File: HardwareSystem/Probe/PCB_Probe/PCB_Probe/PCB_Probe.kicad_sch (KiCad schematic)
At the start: 24 parts, among them J1 Conn_01x15, J2 Conn_01x15, U1 TLC555xP, U2 LP2950CZ-3.0/NOPB

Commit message: PCB Probe layout
working on pcb probe layout
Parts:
- removed R7: Photoresistor, KiCADv6:XDCR_161, symbol 161:Photoresistor
- added J3: Conn_01x02_Socket, Connector_PinHeader_2.54mm:PinHeader_1x02_P2.54mm_Vertical, symbol Connector:Conn_01x02_Socket
- added J4: Conn_01x04_Pin, Connector_PinHeader_2.54mm:PinHeader_1x04_P2.54mm_Vertical, symbol Connector:Conn_01x04_Pin
- added TP4: 3.3V GND Testpoint, TestPoint:TestPoint_Pad_D1.0mm, symbol Connector:TestPoint
- A2: now not fitted
- TP1: value 5V Testpoint -> 9V Testpoint
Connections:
- net +3.3V: now also J3.1 (Pin_1), J4.1 (Pin_1)
- net GND: now also J4.2 (Pin_2), TP4.1
- net SCL: now also J4.3 (Pin_3)
- net SDA: now also J4.4 (Pin_4)
- net at R6.2: now also J3.2 (Pin_2)
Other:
- note added: "AHT20 Temp Humd connection"
- moved on the sheet: BT1, C1, C10, C2, C3, C4, C9, D1, J1, J2, R1, R2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

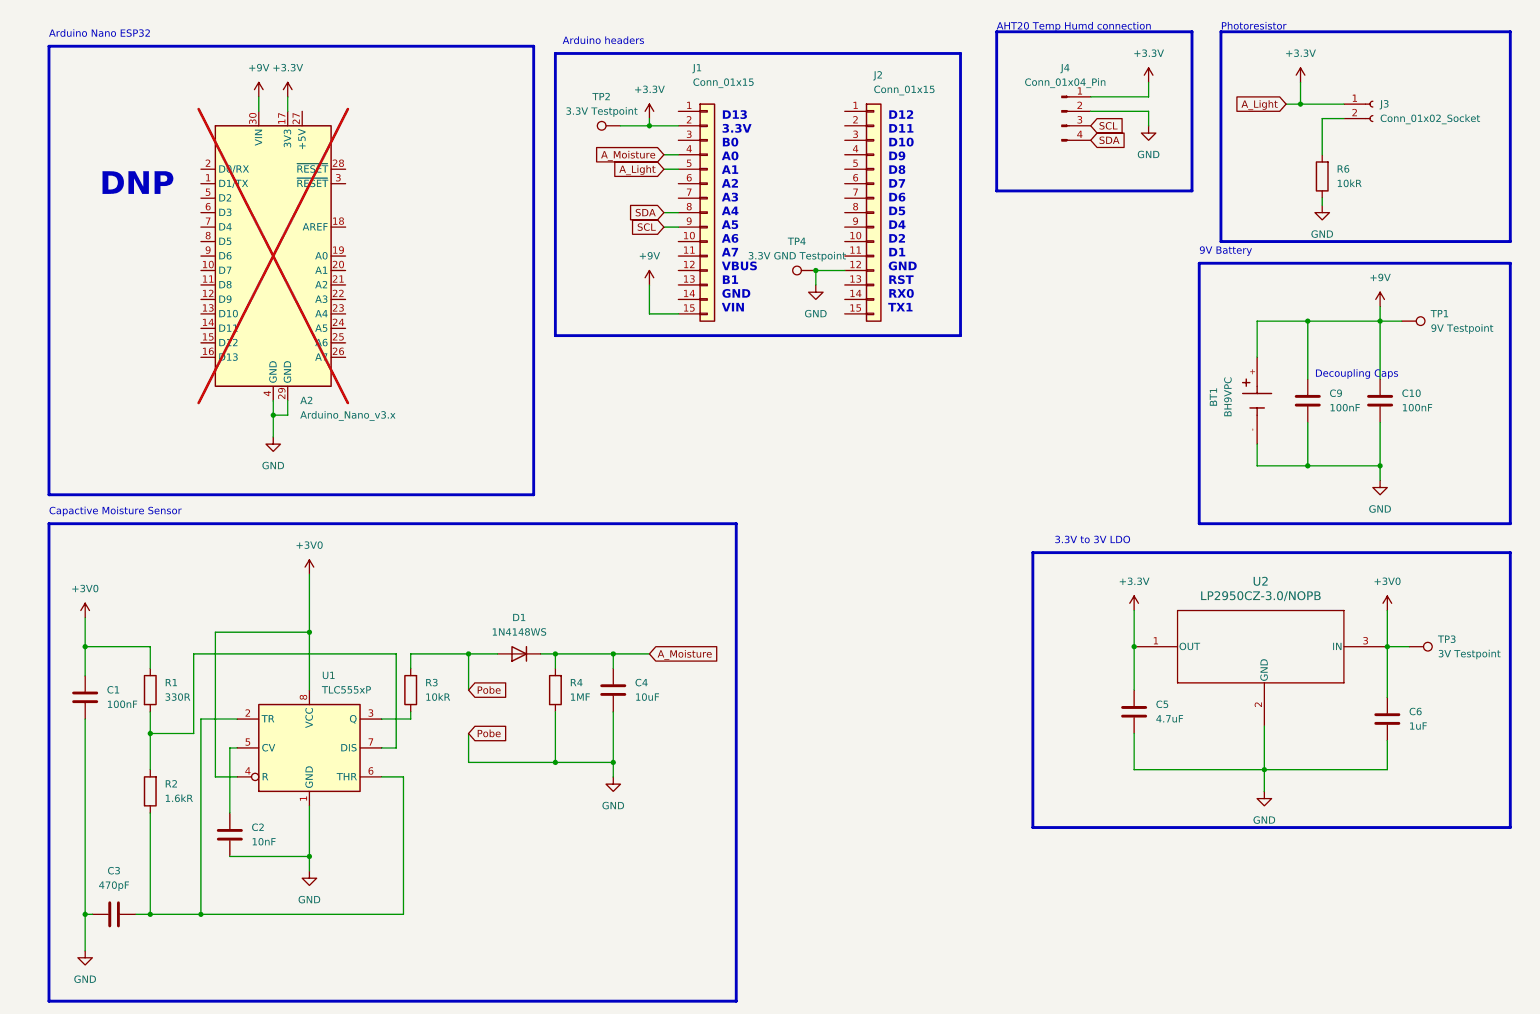
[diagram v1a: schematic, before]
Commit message: Routing and Placement for Probe PCB
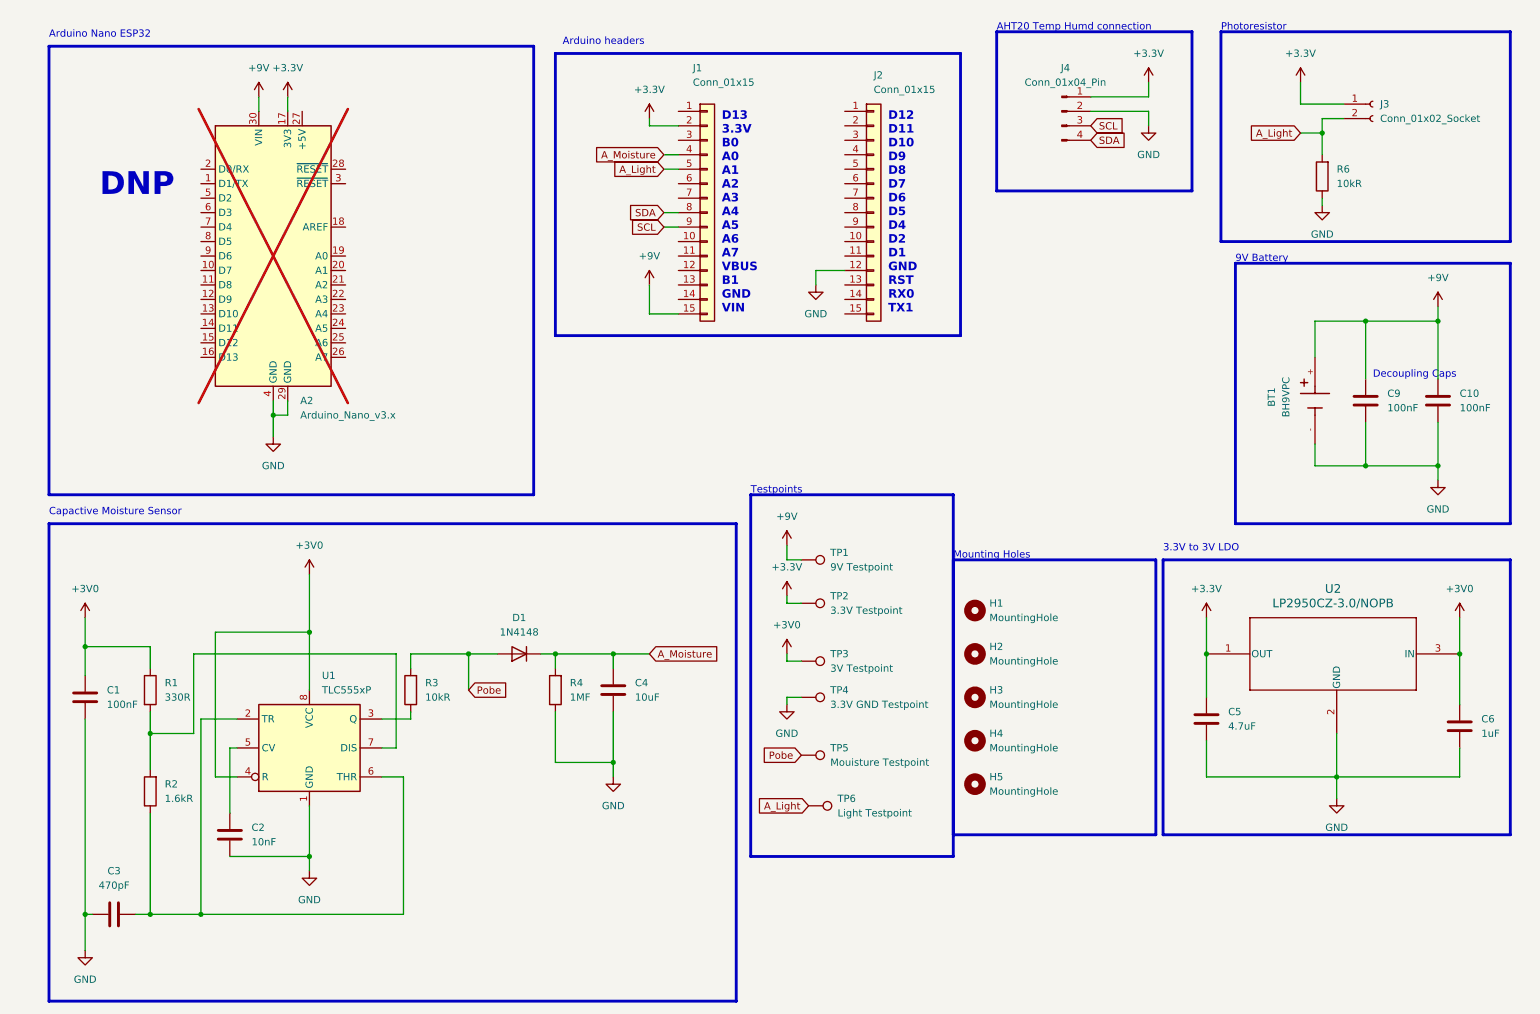
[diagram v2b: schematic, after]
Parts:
- removed D1: 1N4148WS, Diode_SMD:D_SOD-323, symbol Diode:1N4148WS
- added D1: 1N4148, Diode_THT:D_DO-35_SOD27_P7.62mm_Horizontal, symbol Diode:1N4148
- added H1, H2, H3, H4, H5: MountingHole, MountingHole:MountingHole_3.2mm_M3, symbol Mechanical:MountingHole
- added TP5: Mouisture Testpoint, TestPoint:TestPoint_Pad_D1.0mm, symbol Connector:TestPoint
- added TP6: Light Testpoint, TestPoint:TestPoint_Pad_D1.0mm, symbol Connector:TestPoint
- A2: now left out of the parts list
- C1, C10, C2, C3, C4, C5, C6, C9: footprint Capacitor_THT:C_Disc_D3.0mm_W1.6mm_P2.50mm -> Capacitor_THT:C_Disc_D4.7mm_W2.5mm_P5.00mm
- R1, R2, R3, R4, R6: footprint Resistor_THT:R_Axial_DIN0204_L3.6mm_D1.6mm_P5.08mm_Horizontal -> Resistor_THT:R_Axial_DIN0207_L6.3mm_D2.5mm_P10.16mm_Horizontal
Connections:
- net +3.3V: no longer J1.5 (Pin_5)
- net A_Moisture: now also D1.1 (K)
- net GND: no longer R3.2
- net A_Light: now reaches J3.2 (Pin_2), R6.2
- net A_Light: now also J1.5 (Pin_5), TP6.1
- new net Pobe: D1.2 (A), R3.2, TP5.1
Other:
- note added: "Mounting Holes"
- note added: "Testpoints"
- moved on the sheet: BT1, C10, C5, C6, C9, TP2, U2

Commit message: updated Probe schematic look
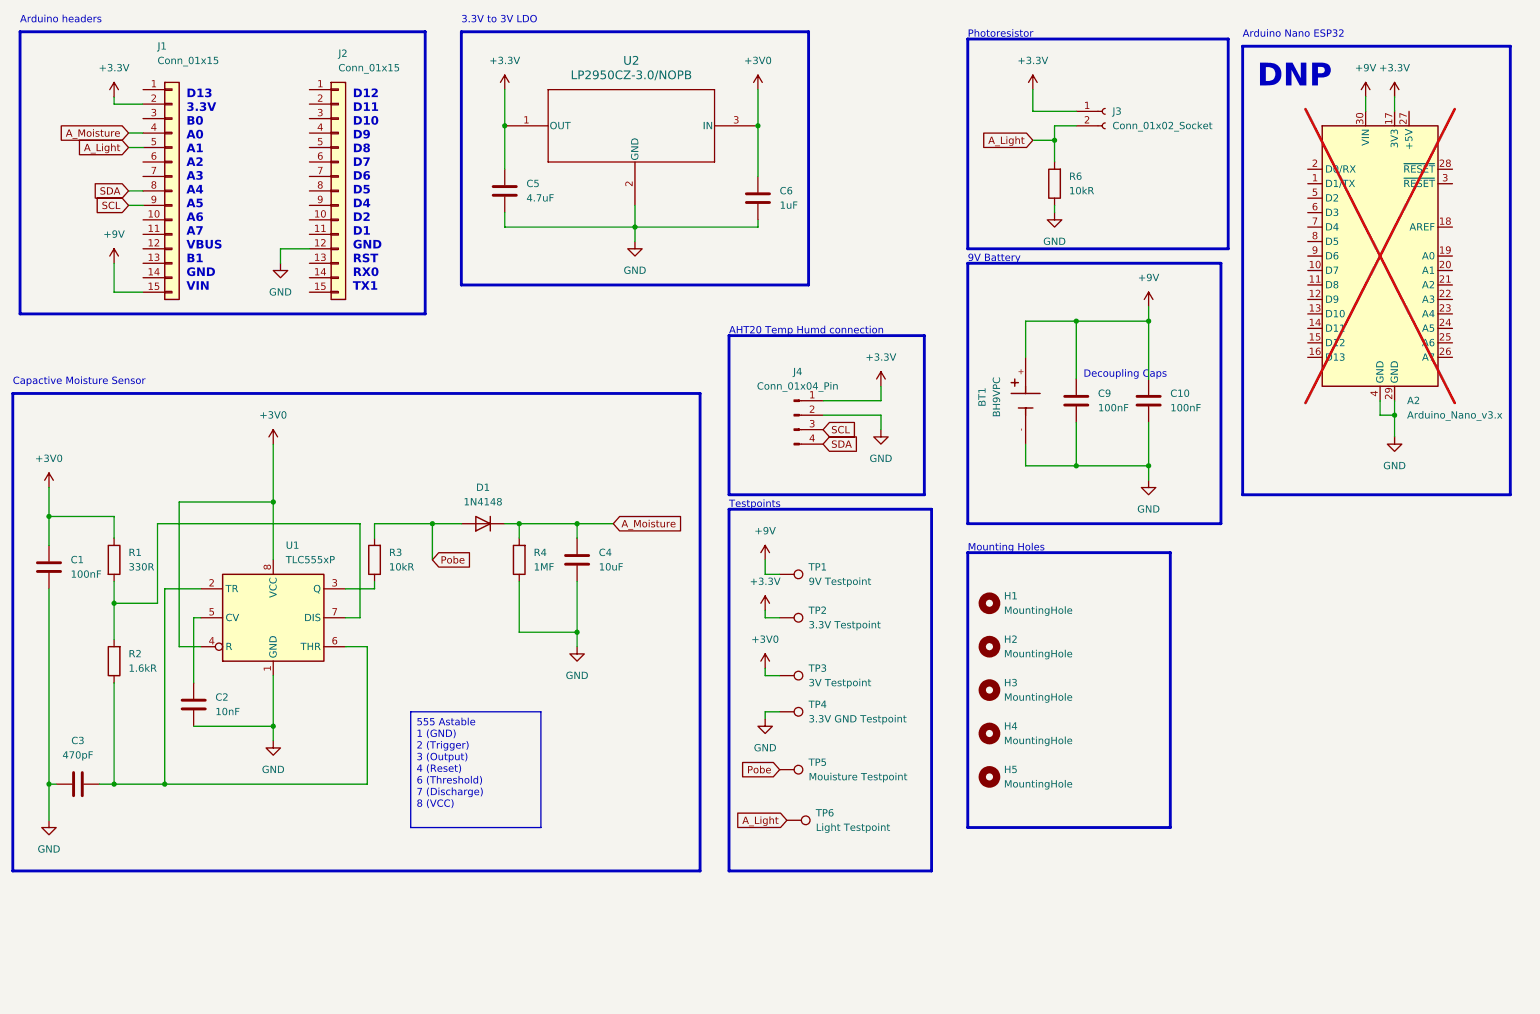
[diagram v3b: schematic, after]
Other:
- moved on the sheet: A2, BT1, C1, C10, C2, C3, C4, C5, C6, C9, D1, H1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

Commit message: updated ground plane footprint
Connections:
- net Pobe renamed Probe
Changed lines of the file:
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@@
     )
   )
-  (global_label "Pobe" (shape input) (at 154.94 147.32 180) (fields_autoplaced)
+  (global_label "Probe" (shape input) (at 154.94 147.32 180) (fields_autoplaced)
     (effects (font (size 1.27 1.27)) (justify right))
-    (property "Intersheetrefs" "${INTERSHEET_REFS}" (at 147.2982 147.32 0)
+    (property "Intersheetrefs" "${INTERSHEET_REFS}" (at 146.512 147.32 0)
       (effects (font (size 1.27 1.27)) (justify right) hide)
     )
@@
     )
   )
-  (global_label "Pobe" (shape input) (at 93.98 110.49 0) (fields_autoplaced)
+  (global_label "Probe" (shape input) (at 93.98 110.49 0) (fields_autoplaced)
     (effects (font (size 1.27 1.27)) (justify left))
-    (property "Intersheetrefs" "${INTERSHEET_REFS}" (at 101.6218 110.49 0)
+    (property "Intersheetrefs" "${INTERSHEET_REFS}" (at 102.408 110.49 0)
       (effects (font (size 1.27 1.27)) (justify left) hide)
     )

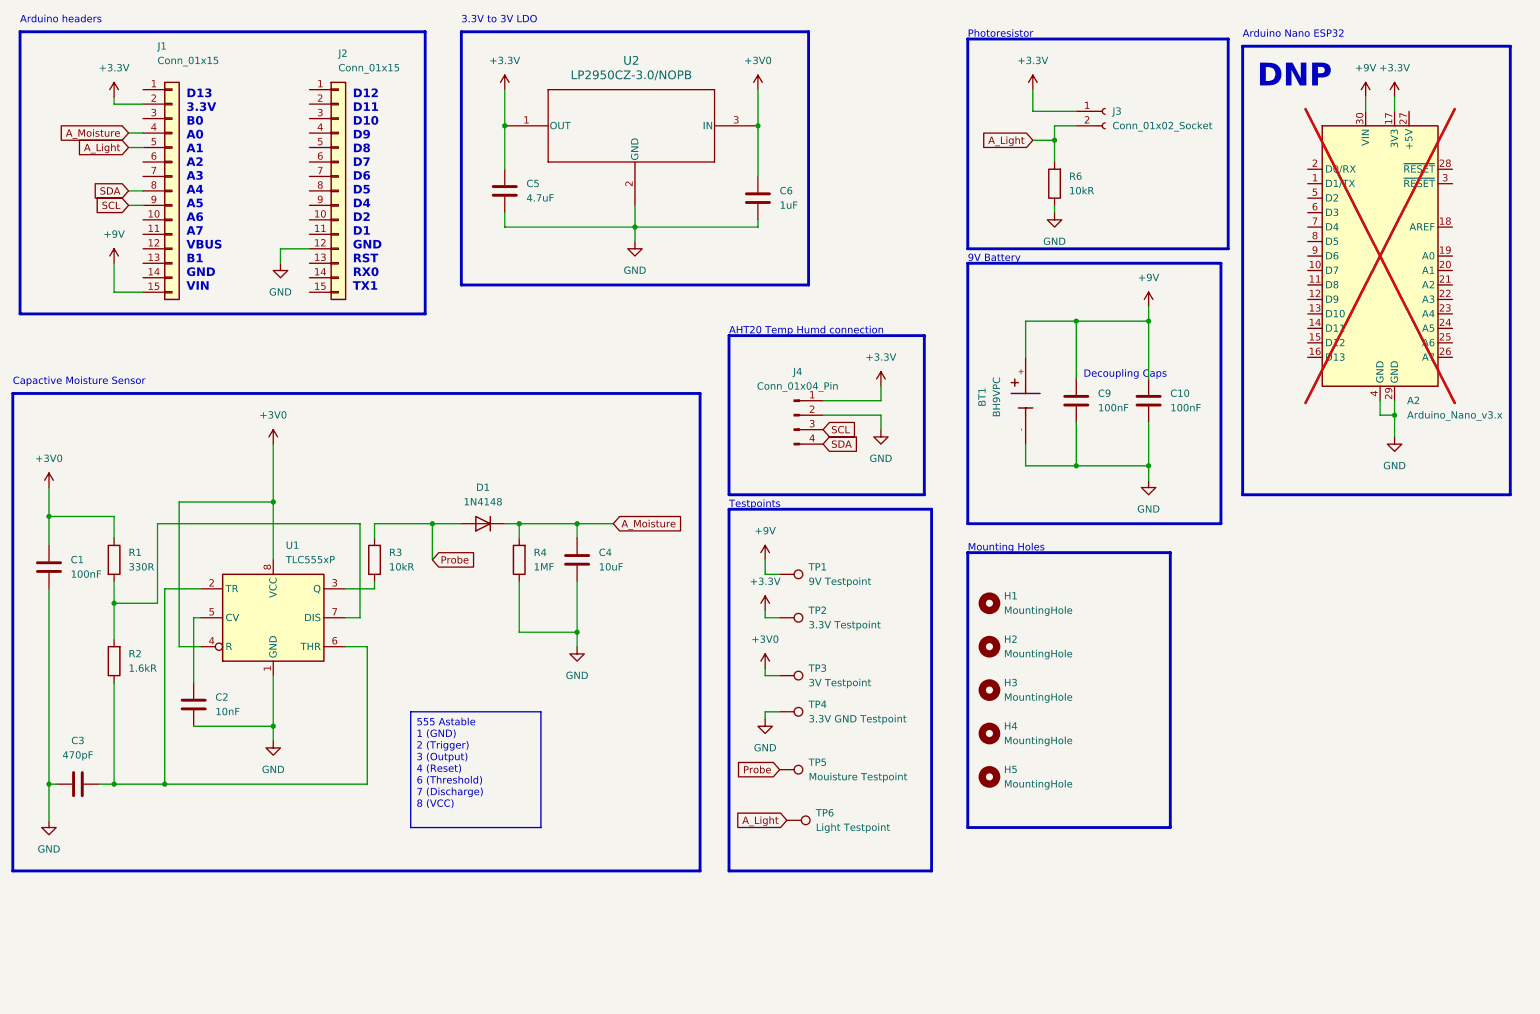
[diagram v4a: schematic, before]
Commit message: removed redundant 3V LDO
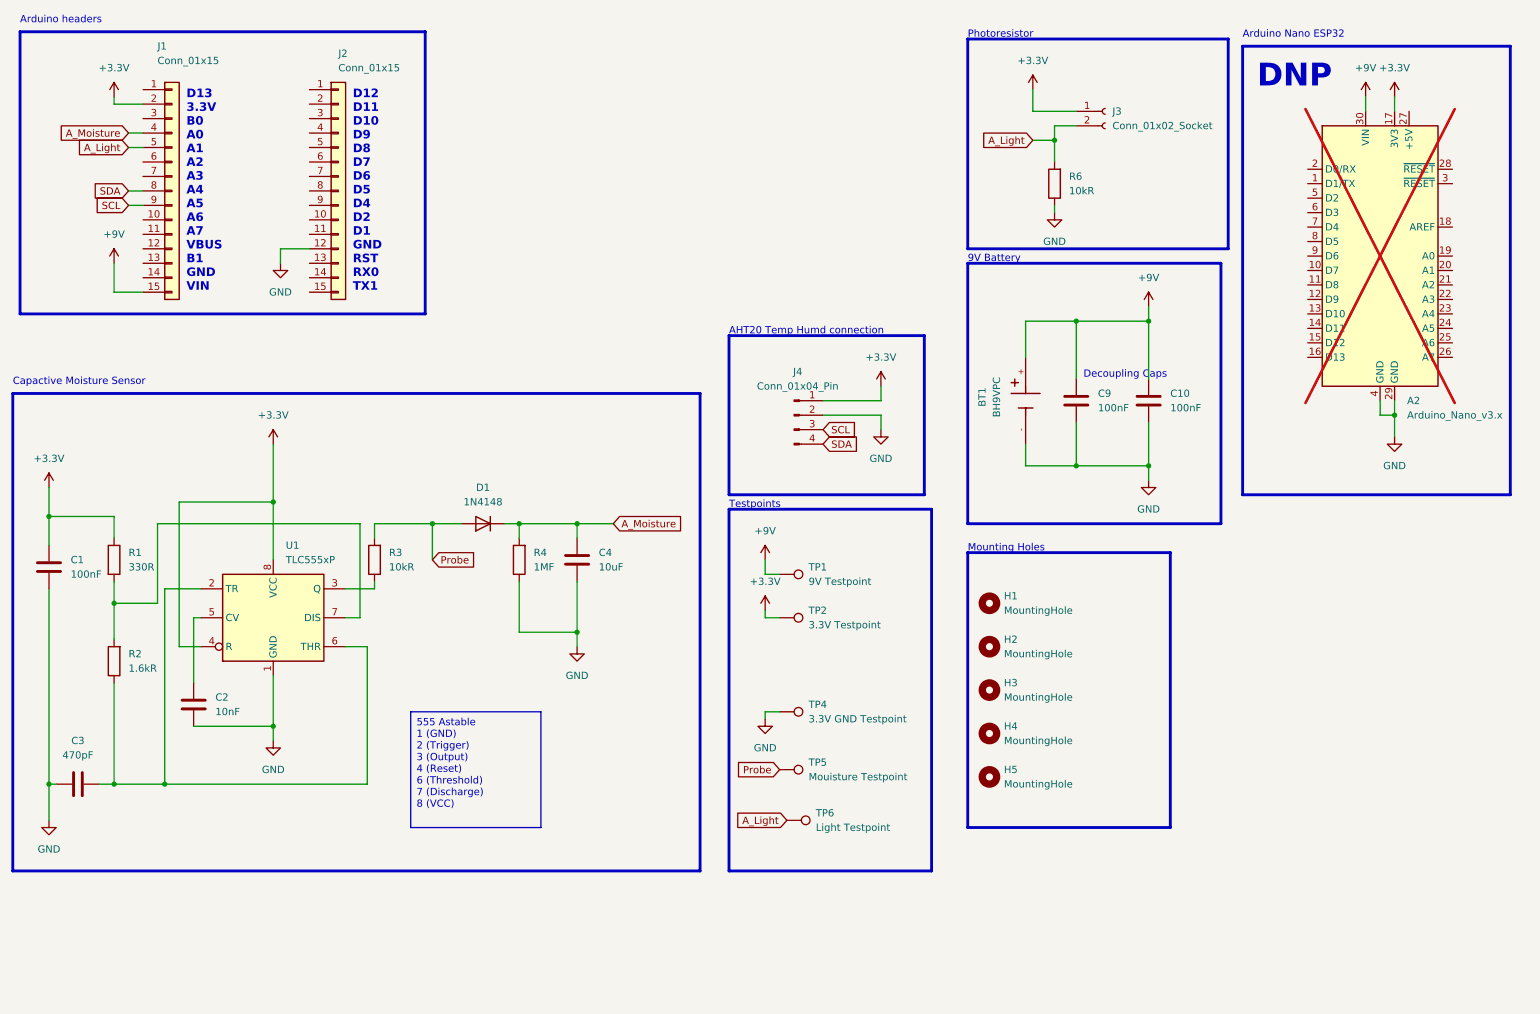
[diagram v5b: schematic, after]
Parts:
- removed C5: 4.7uF, Capacitor_THT:C_Disc_D4.7mm_W2.5mm_P5.00mm, symbol Device:C
- removed C6: 1uF, Capacitor_THT:C_Disc_D4.7mm_W2.5mm_P5.00mm, symbol Device:C
- removed TP3: 3V Testpoint, TestPoint:TestPoint_Pad_D1.0mm, symbol Connector:TestPoint
- removed U2: LP2950CZ-3.0/NOPB, Z03A_TEX, symbol 2024-02-28_23-11-38:LP2950CZ-3.0_NOPB
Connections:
- net +3V0 is gone; now on net +3.3V: C1.2, R1.1, U1.4 (R), U1.8 (VCC)
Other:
- note removed: "3.3V to 3V LDO"
